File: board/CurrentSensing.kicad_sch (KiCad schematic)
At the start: 12 parts, among them IC1 ACS37010LLZATR-030B3, IC2 ACS37010LLZATR-030B3, IC3 ACS37010LLZATR-030B3, IC4 ACS37010LLZATR-030B3, IC5 ACS37010LLZATR-030B3, IC6 ACS37010LLZATR-030B3

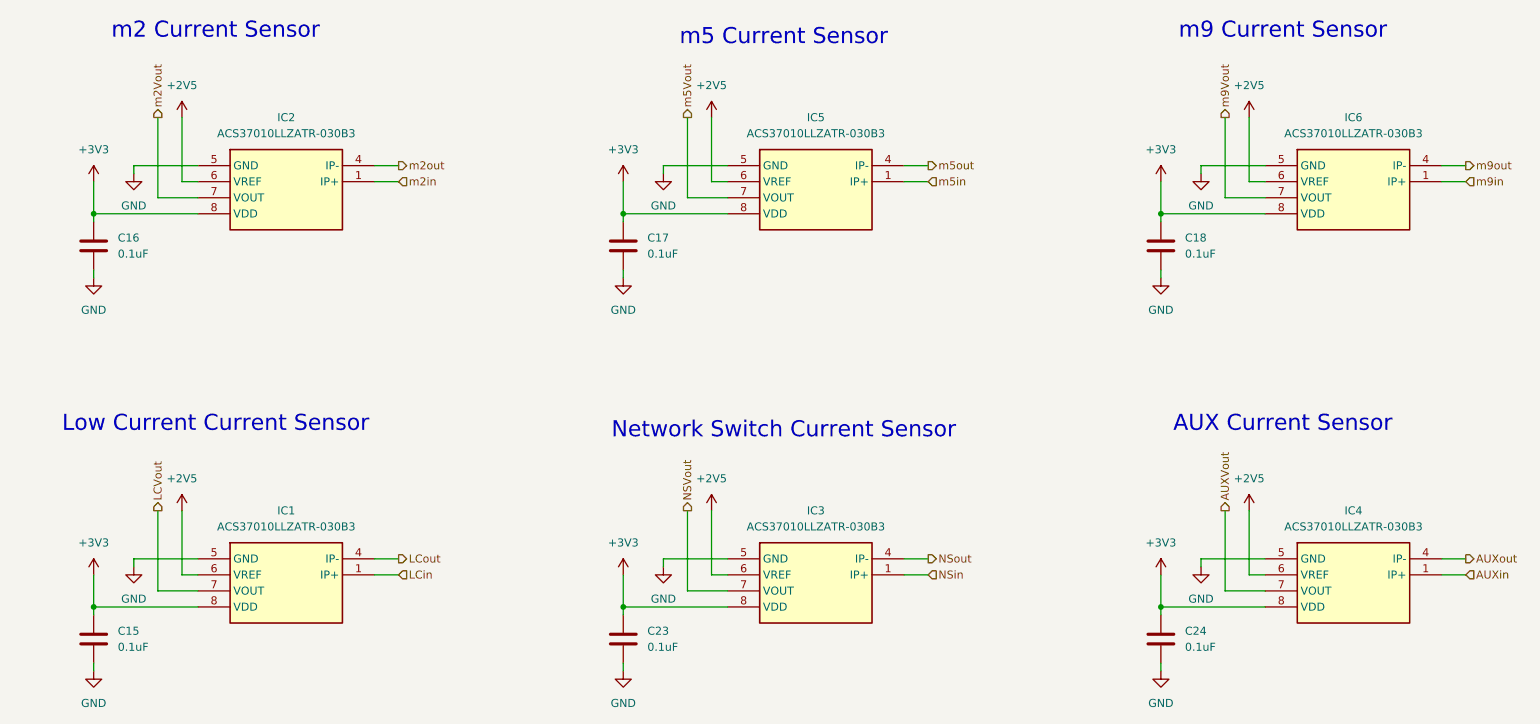
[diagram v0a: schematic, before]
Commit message: Voltage Dividers on Current Sensors
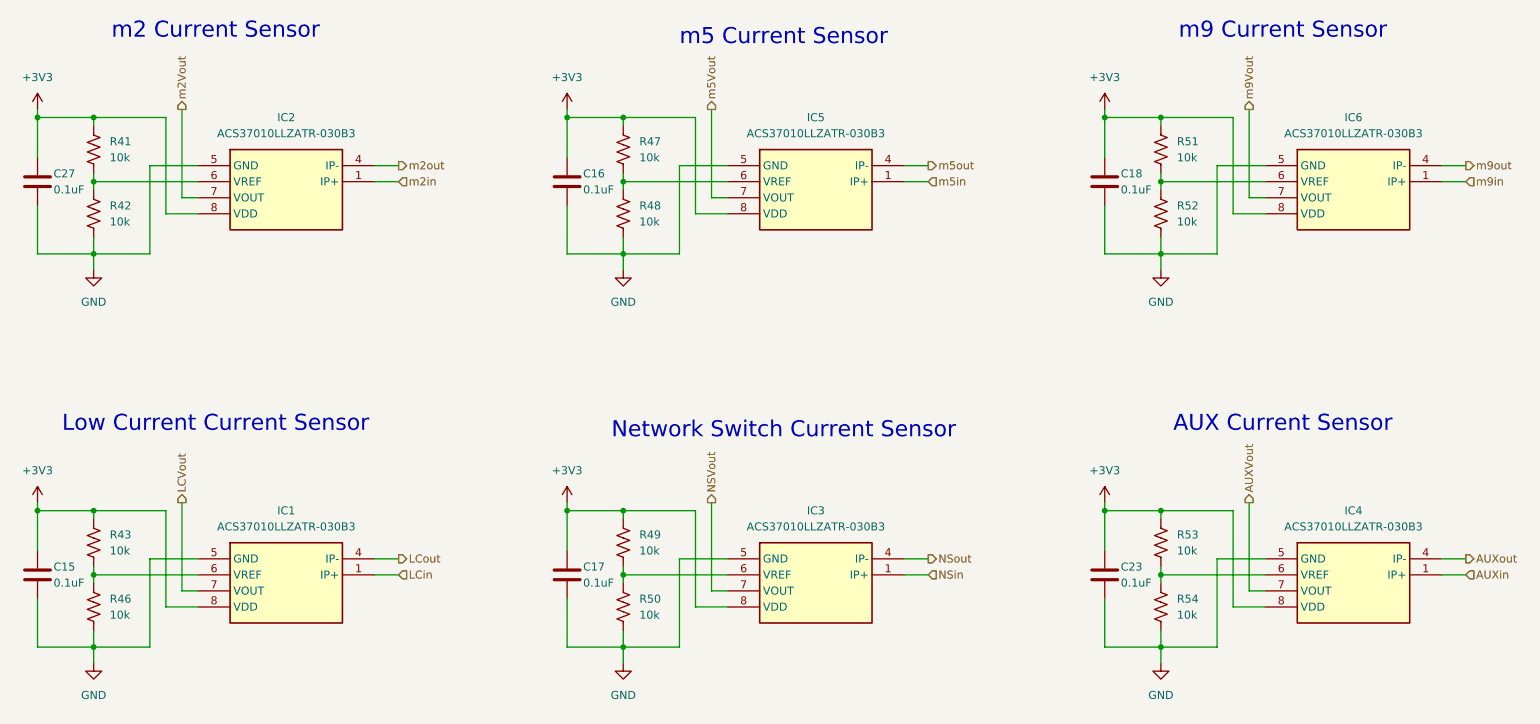
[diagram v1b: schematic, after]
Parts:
- removed C24: 0.1uF, symbol Device:C
- added C27: 0.1uF, symbol Device:C
- added R41, R42, R43, R46, R47, R48, R49, R50, R51, R52, R53, R54: 10k, symbol Device:R_US
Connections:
- net +3V3: now also C27.1, R41.1, R43.1, R47.1, R49.1, R51.1, R53.1
- net GND: now also C27.2, R42.2, R46.2, R48.2, R50.2, R52.2, R54.2
- removed net +2V5: IC1.6 (VREF), IC2.6 (VREF), IC3.6 (VREF), IC4.6 (VREF), IC5.6 (VREF), IC6.6 (VREF)
- new net: IC5.6 (VREF), R47.2, R48.1
- new net: IC1.6 (VREF), R43.2, R46.1
- new net: IC3.6 (VREF), R49.2, R50.1
- new net: IC4.6 (VREF), R53.2, R54.1
- new net: IC2.6 (VREF), R41.2, R42.1
- new net: IC6.6 (VREF), R51.2, R52.1

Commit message: More footprints added
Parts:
- C15, C16, C17, C18, C23, C27: footprint (none) -> Capacitor_SMD:C_0603_1608Metric
- IC1, IC2, IC3, IC4, IC5, IC6: footprint ACS37010LLZATR050B5 -> (none)
- R41, R42, R43, R46, R47, R48, R49, R50, R51, R52, R53, R54: footprint (none) -> Resistor_SMD:R_0603_1608Metric
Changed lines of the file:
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@@
 			)
 		)
-		(property "Footprint" ""
+		(property "Footprint" "Capacitor_SMD:C_0603_1608Metric"
 			(at 36.5252 123.19 0)
 			(effects
@@
 			)
 		)
-		(property "Footprint" ""
+		(property "Footprint" "Resistor_SMD:R_0603_1608Metric"
 			(at 129.286 52.324 90)
 			(effects
@@
 			)
 		)
-		(property "Footprint" "ACS37010LLZATR050B5"
+		(property "Footprint" ""
 			(at 85.09 211.76 0)
 			(effects
@@
 			)
 		)
-		(property "Footprint" ""
+		(property "Footprint" "Resistor_SMD:R_0603_1608Metric"
 			(at 129.286 124.714 90)
 			(effects
@@
 			)
 		)
-		(property "Footprint" ""
+		(property "Footprint" "Resistor_SMD:R_0603_1608Metric"
 			(at 45.466 124.714 90)
 			(effects
@@
 			)
 		)
-		(property "Footprint" ""
+		(property "Footprint" "Resistor_SMD:R_0603_1608Metric"
 			(at 214.376 124.714 90)
 			(effects
@@
 			)
 		)
-		(property "Footprint" ""
+		(property "Footprint" "Resistor_SMD:R_0603_1608Metric"
 			(at 45.466 62.484 90)
 			(effects
@@
 			)
 		)
-		(property "Footprint" ""
+		(property "Footprint" "Capacitor_SMD:C_0603_1608Metric"
 			(at 120.3452 60.96 0)
 			(effects
@@
 			)
 		)
-		(property "Footprint" ""
+		(property "Footprint" "Capacitor_SMD:C_0603_1608Metric"
 			(at 205.4352 123.19 0)
 			(effects
@@
 			)
 		)
-		(property "Footprint" ""
+		(property "Footprint" "Resistor_SMD:R_0603_1608Metric"
 			(at 214.376 62.484 90)
 			(effects
@@
 			)
 		)
-		(property "Footprint" "ACS37010LLZATR050B5"
+		(property "Footprint" ""
 			(at 254 211.76 0)
 			(effects
@@
 			)
 		)
-		(property "Footprint" ""
+		(property "Footprint" "Capacitor_SMD:C_0603_1608Metric"
 			(at 36.5252 60.96 0)
 			(effects
@@
 			)
 		)
-		(property "Footprint" ""
+		(property "Footprint" "Capacitor_SMD:C_0603_1608Metric"
 			(at 120.3452 123.19 0)
 			(effects
@@
 			)
 		)
-		(property "Footprint" ""
+		(property "Footprint" "Resistor_SMD:R_0603_1608Metric"
 			(at 45.466 114.554 90)
 			(effects
@@
 			)
 		)
-		(property "Footprint" ""
+		(property "Footprint" "Resistor_SMD:R_0603_1608Metric"
 			(at 129.286 62.484 90)
 			(effects
@@
 			)
 		)
-		(property "Footprint" ""
+		(property "Footprint" "Capacitor_SMD:C_0603_1608Metric"
 			(at 205.4352 60.96 0)
 			(effects
@@
 			)
 		)
-		(property "Footprint" "ACS37010LLZATR050B5"
+		(property "Footprint" ""
 			(at 254 149.53 0)
 			(effects
@@
 			)
 		)
-		(property "Footprint" ""
+		(property "Footprint" "Resistor_SMD:R_0603_1608Metric"
 			(at 129.286 114.554 90)
 			(effects
@@
 			)
 		)
-		(property "Footprint" "ACS37010LLZATR050B5"
+		(property "Footprint" ""
 			(at 85.09 149.53 0)
 			(effects
@@
 			)
 		)
-		(property "Footprint" "ACS37010LLZATR050B5"
+		(property "Footprint" ""
 			(at 168.91 211.76 0)
 			(effects
@@
 			)
 		)
-		(property "Footprint" ""
+		(property "Footprint" "Resistor_SMD:R_0603_1608Metric"
 			(at 214.376 52.324 90)
 			(effects
@@
 			)
 		)
-		(property "Footprint" "ACS37010LLZATR050B5"
+		(property "Footprint" ""
 			(at 168.91 149.53 0)
 			(effects
@@
 			)
 		)
-		(property "Footprint" ""
+		(property "Footprint" "Resistor_SMD:R_0603_1608Metric"
 			(at 214.376 114.554 90)
 			(effects
@@
 			)
 		)
-		(property "Footprint" ""
+		(property "Footprint" "Resistor_SMD:R_0603_1608Metric"
 			(at 45.466 52.324 90)
 			(effects

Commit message: Changed footprints to handsolder version
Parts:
- C15, C16, C17, C18, C23, C27: footprint Capacitor_SMD:C_0603_1608Metric -> Capacitor_SMD:C_0603_1608Metric_Pad1.08x0.95mm_HandSolder
- R41, R42, R43, R46, R47, R48, R49, R50, R51, R52, R53, R54: footprint Resistor_SMD:R_0603_1608Metric -> Resistor_SMD:R_0603_1608Metric_Pad0.98x0.95mm_HandSolder
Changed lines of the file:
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@@
 			)
 		)
-		(property "Footprint" "Capacitor_SMD:C_0603_1608Metric"
+		(property "Footprint" "Capacitor_SMD:C_0603_1608Metric_Pad1.08x0.95mm_HandSolder"
 			(at 36.5252 123.19 0)
 			(effects
@@
 			)
 		)
-		(property "Footprint" "Resistor_SMD:R_0603_1608Metric"
+		(property "Footprint" "Resistor_SMD:R_0603_1608Metric_Pad0.98x0.95mm_HandSolder"
 			(at 129.286 52.324 90)
 			(effects
@@
 			)
 		)
-		(property "Footprint" "Resistor_SMD:R_0603_1608Metric"
+		(property "Footprint" "Resistor_SMD:R_0603_1608Metric_Pad0.98x0.95mm_HandSolder"
 			(at 129.286 124.714 90)
 			(effects
@@
 			)
 		)
-		(property "Footprint" "Resistor_SMD:R_0603_1608Metric"
+		(property "Footprint" "Resistor_SMD:R_0603_1608Metric_Pad0.98x0.95mm_HandSolder"
 			(at 45.466 124.714 90)
 			(effects
@@
 			)
 		)
-		(property "Footprint" "Resistor_SMD:R_0603_1608Metric"
+		(property "Footprint" "Resistor_SMD:R_0603_1608Metric_Pad0.98x0.95mm_HandSolder"
 			(at 214.376 124.714 90)
 			(effects
@@
 			)
 		)
-		(property "Footprint" "Resistor_SMD:R_0603_1608Metric"
+		(property "Footprint" "Resistor_SMD:R_0603_1608Metric_Pad0.98x0.95mm_HandSolder"
 			(at 45.466 62.484 90)
 			(effects
@@
 			)
 		)
-		(property "Footprint" "Capacitor_SMD:C_0603_1608Metric"
+		(property "Footprint" "Capacitor_SMD:C_0603_1608Metric_Pad1.08x0.95mm_HandSolder"
 			(at 120.3452 60.96 0)
 			(effects
@@
 			)
 		)
-		(property "Footprint" "Capacitor_SMD:C_0603_1608Metric"
+		(property "Footprint" "Capacitor_SMD:C_0603_1608Metric_Pad1.08x0.95mm_HandSolder"
 			(at 205.4352 123.19 0)
 			(effects
@@
 			)
 		)
-		(property "Footprint" "Resistor_SMD:R_0603_1608Metric"
+		(property "Footprint" "Resistor_SMD:R_0603_1608Metric_Pad0.98x0.95mm_HandSolder"
 			(at 214.376 62.484 90)
 			(effects
@@
 			)
 		)
-		(property "Footprint" "Capacitor_SMD:C_0603_1608Metric"
+		(property "Footprint" "Capacitor_SMD:C_0603_1608Metric_Pad1.08x0.95mm_HandSolder"
 			(at 36.5252 60.96 0)
 			(effects
@@
 			)
 		)
-		(property "Footprint" "Capacitor_SMD:C_0603_1608Metric"
+		(property "Footprint" "Capacitor_SMD:C_0603_1608Metric_Pad1.08x0.95mm_HandSolder"
 			(at 120.3452 123.19 0)
 			(effects
@@
 			)
 		)
-		(property "Footprint" "Resistor_SMD:R_0603_1608Metric"
+		(property "Footprint" "Resistor_SMD:R_0603_1608Metric_Pad0.98x0.95mm_HandSolder"
 			(at 45.466 114.554 90)
 			(effects
@@
 			)
 		)
-		(property "Footprint" "Resistor_SMD:R_0603_1608Metric"
+		(property "Footprint" "Resistor_SMD:R_0603_1608Metric_Pad0.98x0.95mm_HandSolder"
 			(at 129.286 62.484 90)
 			(effects
@@
 			)
 		)
-		(property "Footprint" "Capacitor_SMD:C_0603_1608Metric"
+		(property "Footprint" "Capacitor_SMD:C_0603_1608Metric_Pad1.08x0.95mm_HandSolder"
 			(at 205.4352 60.96 0)
 			(effects
@@
 			)
 		)
-		(property "Footprint" "Resistor_SMD:R_0603_1608Metric"
+		(property "Footprint" "Resistor_SMD:R_0603_1608Metric_Pad0.98x0.95mm_HandSolder"
 			(at 129.286 114.554 90)
 			(effects
@@
 			)
 		)
-		(property "Footprint" "Resistor_SMD:R_0603_1608Metric"
+		(property "Footprint" "Resistor_SMD:R_0603_1608Metric_Pad0.98x0.95mm_HandSolder"
 			(at 214.376 52.324 90)
 			(effects
@@
 			)
 		)
-		(property "Footprint" "Resistor_SMD:R_0603_1608Metric"
+		(property "Footprint" "Resistor_SMD:R_0603_1608Metric_Pad0.98x0.95mm_HandSolder"
 			(at 214.376 114.554 90)
 			(effects
@@
 			)
 		)
-		(property "Footprint" "Resistor_SMD:R_0603_1608Metric"
+		(property "Footprint" "Resistor_SMD:R_0603_1608Metric_Pad0.98x0.95mm_HandSolder"
 			(at 45.466 52.324 90)
 			(effects

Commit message: Assigned Current Sensor Footprints
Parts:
- IC1, IC2, IC3, IC4, IC5, IC6: footprint (none) -> ACS37010LLZATR-030B3:IC_ACS37030LLZATR-040B3
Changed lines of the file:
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@@
 			)
 		)
-		(property "Footprint" ""
+		(property "Footprint" "ACS37010LLZATR-030B3:IC_ACS37030LLZATR-040B3"
 			(at 85.09 211.76 0)
 			(effects
@@
 			)
 		)
-		(property "Footprint" ""
+		(property "Footprint" "ACS37010LLZATR-030B3:IC_ACS37030LLZATR-040B3"
 			(at 254 211.76 0)
 			(effects
@@
 			)
 		)
-		(property "Footprint" ""
+		(property "Footprint" "ACS37010LLZATR-030B3:IC_ACS37030LLZATR-040B3"
 			(at 254 149.53 0)
 			(effects
@@
 			)
 		)
-		(property "Footprint" ""
+		(property "Footprint" "ACS37010LLZATR-030B3:IC_ACS37030LLZATR-040B3"
 			(at 85.09 149.53 0)
 			(effects
@@
 			)
 		)
-		(property "Footprint" ""
+		(property "Footprint" "ACS37010LLZATR-030B3:IC_ACS37030LLZATR-040B3"
 			(at 168.91 211.76 0)
 			(effects
@@
 			)
 		)
-		(property "Footprint" ""
+		(property "Footprint" "ACS37010LLZATR-030B3:IC_ACS37030LLZATR-040B3"
 			(at 168.91 149.53 0)
 			(effects

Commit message: Finally assigned the footprints for current sensor, led, poe
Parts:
- IC1, IC2, IC3, IC4, IC5, IC6: footprint ACS37010LLZATR-030B3:IC_ACS37030LLZATR-040B3 -> PowerManagementBoard:IC_ACS37030LLZATR-040B3
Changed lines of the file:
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@@
 			)
 		)
-		(property "Footprint" "ACS37010LLZATR-030B3:IC_ACS37030LLZATR-040B3"
+		(property "Footprint" "PowerManagementBoard:IC_ACS37030LLZATR-040B3"
 			(at 85.09 211.76 0)
 			(effects
@@
 			)
 		)
-		(property "Footprint" "ACS37010LLZATR-030B3:IC_ACS37030LLZATR-040B3"
+		(property "Footprint" "PowerManagementBoard:IC_ACS37030LLZATR-040B3"
 			(at 254 211.76 0)
 			(effects
@@
 			)
 		)
-		(property "Footprint" "ACS37010LLZATR-030B3:IC_ACS37030LLZATR-040B3"
+		(property "Footprint" "PowerManagementBoard:IC_ACS37030LLZATR-040B3"
 			(at 254 149.53 0)
 			(effects
@@
 			)
 		)
-		(property "Footprint" "ACS37010LLZATR-030B3:IC_ACS37030LLZATR-040B3"
+		(property "Footprint" "PowerManagementBoard:IC_ACS37030LLZATR-040B3"
 			(at 85.09 149.53 0)
 			(effects
@@
 			)
 		)
-		(property "Footprint" "ACS37010LLZATR-030B3:IC_ACS37030LLZATR-040B3"
+		(property "Footprint" "PowerManagementBoard:IC_ACS37030LLZATR-040B3"
 			(at 168.91 211.76 0)
 			(effects
@@
 			)
 		)
-		(property "Footprint" "ACS37010LLZATR-030B3:IC_ACS37030LLZATR-040B3"
+		(property "Footprint" "PowerManagementBoard:IC_ACS37030LLZATR-040B3"
 			(at 168.91 149.53 0)
 			(effects

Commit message: experimented with layout
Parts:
- removed C16: 0.1uF, Capacitor_SMD:C_0603_1608Metric_Pad1.08x0.95mm_HandSolder, symbol Device:C
- removed IC5: ACS37010LLZATR-030B3, PowerManagementBoard:IC_ACS37030LLZATR-040B3, symbol ACS37010LLZATR-030B3:ACS37010LLZATR-030B3
- removed R41, R42, R43, R46, R47, R48, R49, R50, R51, R52, R53, R54: 10k, Resistor_SMD:R_0603_1608Metric_Pad0.98x0.95mm_HandSolder, symbol Device:R_US
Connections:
- no-connect marks 0 -> 5
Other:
- note removed: "m5 Current Sensor"

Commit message: do basically everything
12 hours of our life
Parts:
- added TP5: TestPoint, Connector_Pin:Pin_D1.1mm_L10.2mm_W3.5mm_Flat, symbol Connector:TestPoint
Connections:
- net LCin: now also TP5.1
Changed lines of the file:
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@@
+	)
+	(junction
+		(at 90.17 119.38)
+		(diameter 0)
+		(color 0 0 0 0)
 	)
 	(junction
@@
 	(wire
 		(pts
-			(xy 88.9 119.38) (xy 92.71 119.38)
+			(xy 88.9 119.38) (xy 90.17 119.38)
 		)
 		(stroke
@@
 		(pts
 			(xy 53.34 116.84) (xy 60.96 116.84)
+		)
+		(stroke
+			(width 0)
+			(type default)
+		)
+	)
+	(wire
+		(pts
+			(xy 90.17 119.38) (xy 92.71 119.38)
 		)
 		(stroke
@@
 					(unit 1)
 				)
+			)
+		)
+	)
+	(symbol
+		(lib_id "Connector:TestPoint")
+		(at 90.17 119.38 180)
+		(unit 1)
+		(exclude_from_sim no)
+		(in_bom yes)
+		(on_board yes)
+		(dnp no)
+		(fields_autoplaced yes)
+		(property "Reference" "TP5"
+			(at 92.71 121.4119 0)
+			(effects
+				(font
+					(size 1.27 1.27)
+				)
+				(justify right)
+			)
+		)
+		(property "Value" "TestPoint"
+			(at 92.71 123.9519 0)
+			(effects
+				(font
+					(size 1.27 1.27)
+				)
+				(justify right)
+			)
+		)
+		(property "Footprint" "Connector_Pin:Pin_D1.1mm_L10.2mm_W3.5mm_Flat"
+			(at 85.09 119.38 0)
+			(effects
+				(font
+					(size 1.27 1.27)
+				)
+				(hide yes)
+			)
+		)
+		(property "Datasheet" "~"
+			(at 85.09 119.38 0)
+			(effects
+				(font
+					(size 1.27 1.27)
+				)
+				(hide yes)
+			)
+		)
+		(property "Description" "test point"
+			(at 90.17 119.38 0)
+			(effects
+				(font
+					(size 1.27 1.27)
+				)
+				(hide yes)
+			)
+		)
+		(pin "1"
+		)
+		(instances
+			(project "PowerManagementBoard"
+				(path "/7eaa639d-7062-45e7-be05-1c2855431307/553f5510-83a4-4a32-8cf5-5f8ae000bb74"
+					(reference "TP5")
+					(unit 1)
+				)

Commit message: 17 hours of our lives
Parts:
- TP5: footprint Connector_Pin:Pin_D1.1mm_L10.2mm_W3.5mm_Flat -> TestPoint:TestPoint_Pad_D1.0mm
